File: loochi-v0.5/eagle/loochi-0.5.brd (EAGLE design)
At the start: 68.8 x 63.8 mm, 55 parts, among them IC1 ATTINY61M, J1 SPI_PRG, J2 POWER_JACKSMD, P1 53047-0610, Q1 PMN25ENSOT457, Q2 PMN25ENSOT457, Q3 PMN25ENSOT457, U1 LZ4-00MC00BIGPADS, U2 APDS-9007, X1 SMA-SMD

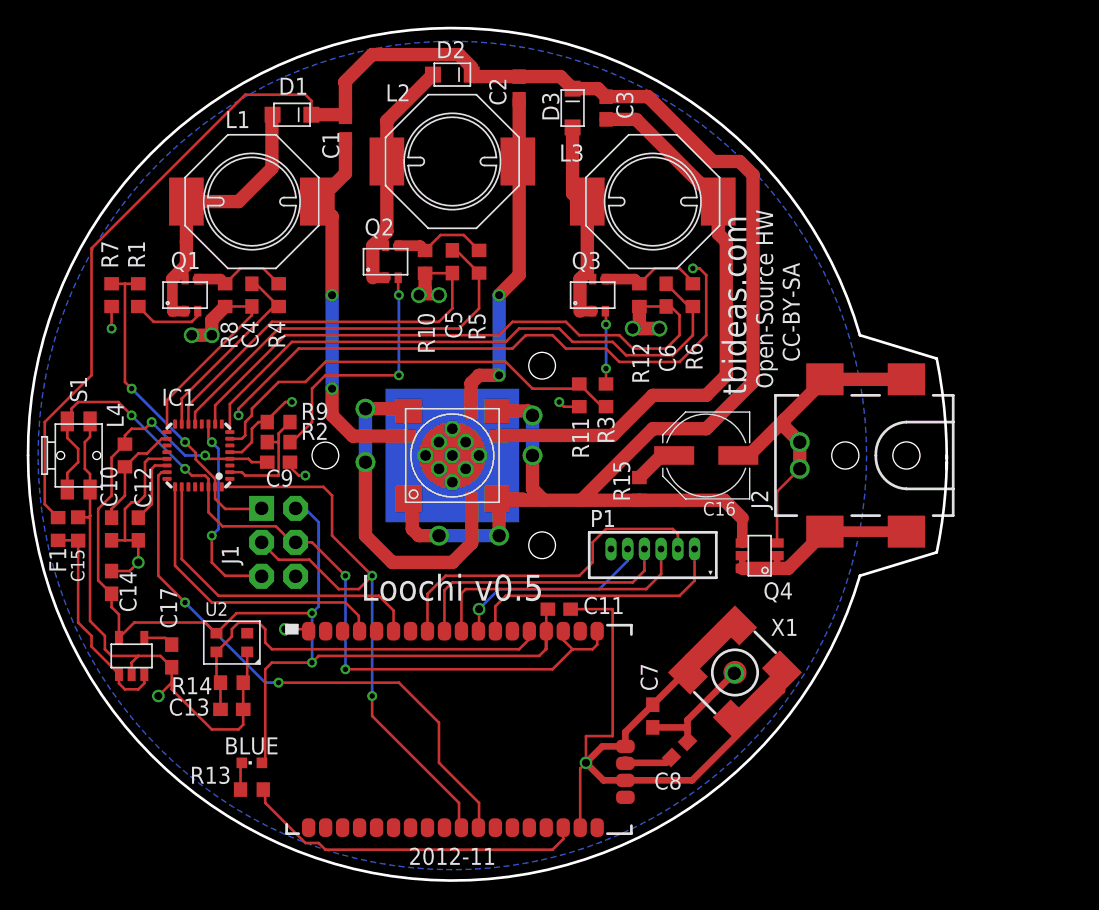
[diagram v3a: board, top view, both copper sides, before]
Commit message: Commiting board 0.5 as ordered from Oshpark.com
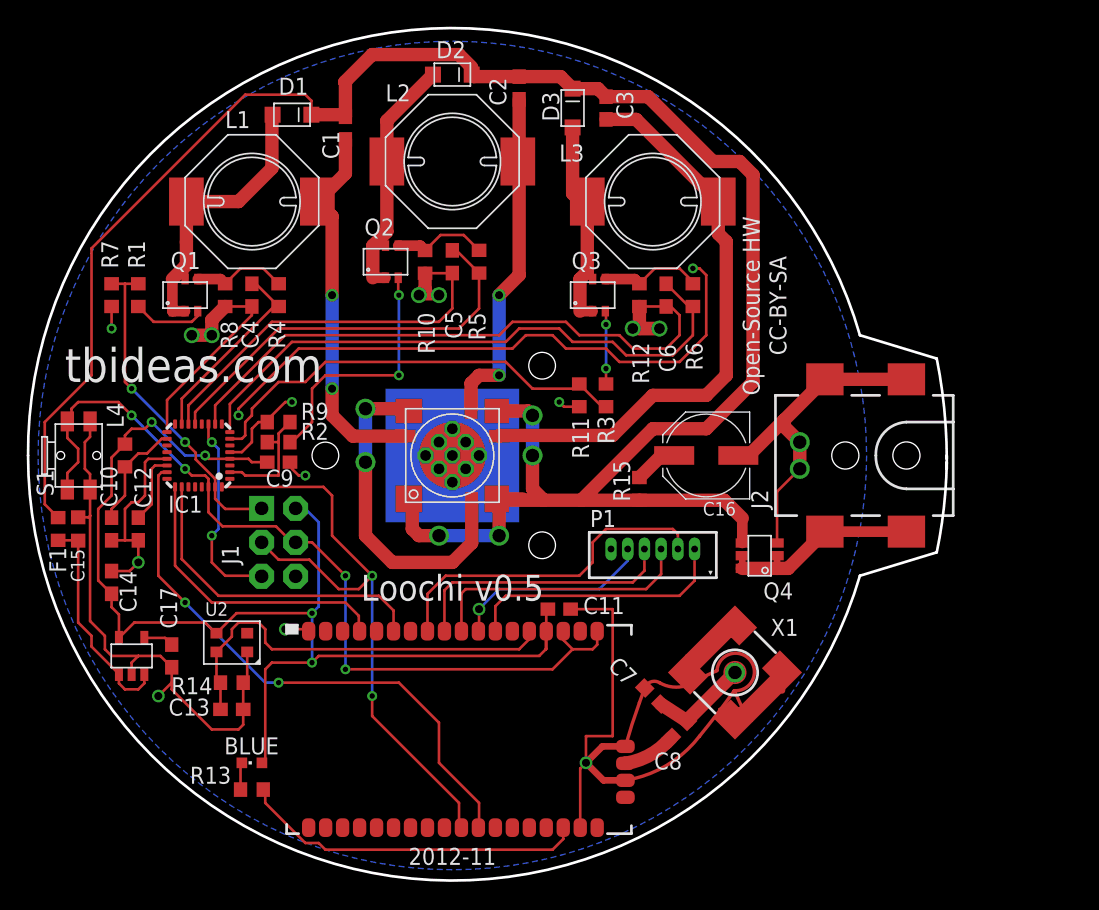
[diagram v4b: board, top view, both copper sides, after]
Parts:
- moved C7 1.50 mm to (47.0, 14.0), turned to 135 degrees
- moved C8 1.50 mm to (49.0, 11.5)
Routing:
- net GND: track 312.9 -> 317.9 mm
- net N$15: track 9.29 -> 7.51 mm, vias 0 -> 1
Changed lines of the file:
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@@
 <hole x="38.718" y="25.282" drill="2"/>
 <text x="32" y="22.1" size="1.9304" layer="21" font="vector" align="center">Loochi v0.5</text>
-<text x="54" y="36.5" size="1.778" layer="21" rot="R90">tbideas.com</text>
-<text x="56" y="37" size="1.27" layer="21" rot="R90">Open-Source HW</text>
-<text x="58" y="39" size="1.27" layer="21" rot="R90">CC-BY-SA</text>
+<text x="3" y="37.5" size="2.54" layer="21" font="vector">tbideas.com</text>
+<text x="55" y="36.5" size="1.27" layer="21" rot="R90">Open-Source HW</text>
+<text x="57" y="39.5" size="1.27" layer="21" rot="R90">CC-BY-SA</text>
 <text x="32" y="2" size="1.27" layer="21" font="vector" align="center">2012-11</text>
 <wire x1="0.25" y1="32" x2="62.5" y2="23" width="0.2" layer="20" curve="163.686148"/>
@@
 <attribute name="MF" value="" x="-37.8" y="38.35" size="1.778" layer="27" rot="R180" display="off"/>
 <attribute name="OC_FARNELL" value="unknown" x="-37.8" y="38.35" size="1.778" layer="27" rot="R180" display="off"/>
-<attribute name="NAME" x="10.24" y="35.7206" size="1.27" layer="25" ratio="10"/>
+<attribute name="NAME" x="10.74" y="27.7206" size="1.27" layer="25" ratio="10"/>
 </element>
 <element name="Q1" library="mosfet" package="SOT457" value="PMN25ENSOT457" x="12" y="44" smashed="yes" rot="R90">
@@
 <element name="S1" library="AIRcam" package="TACTSWITCHHORIZONTAL" value="" x="2.69" y="32" smashed="yes" rot="R270">
 <attribute name="PARTNO" value="*" x="11.19" y="39" size="1.778" layer="27" rot="R270" display="off"/>
-<attribute name="NAME" x="3.39" y="37.95" size="1.27" layer="25" rot="R270"/>
+<attribute name="NAME" x="0.89" y="30.95" size="1.27" layer="25" rot="R270"/>
 <attribute name="VALUE" x="0.19" y="34.25" size="0.8128" layer="27" ratio="10" rot="R270"/>
 </element>
@@
 <attribute name="VALUE" x="18.27" y="10.905" size="1.27" layer="27" rot="R180"/>
 </element>
-<element name="C8" library="rcl" package="C0603" value="100n" x="49" y="10" smashed="yes" rot="R45">
-<attribute name="PARTNO" value="*" x="49" y="10" size="1.778" layer="27" rot="R45" display="off"/>
-<attribute name="NAME" x="47.101971875" y="7" size="1.27" layer="25"/>
-</element>
-<element name="C7" library="rcl" package="C0603" value="100n" x="47" y="12.5" smashed="yes" rot="R90">
-<attribute name="PARTNO" value="*" x="47" y="12.5" size="1.778" layer="27" rot="R90" display="off"/>
-<attribute name="NAME" x="47.365" y="14.365" size="1.27" layer="25" rot="R90"/>
+<element name="C8" library="rcl" package="C0603" value="100n" x="49" y="11.5" smashed="yes" rot="R45">
+<attribute name="PARTNO" value="*" x="49" y="11.5" size="1.778" layer="27" rot="R45" display="off"/>
+<attribute name="NAME" x="47.101971875" y="8.5" size="1.27" layer="25"/>
+</element>
+<element name="C7" library="rcl" package="C0603" value="100n" x="47" y="14" smashed="yes" rot="R135">
+<attribute name="PARTNO" value="*" x="47" y="14" size="1.778" layer="27" rot="R135" display="off"/>
+<attribute name="NAME" x="45.9393375" y="15.57684375" size="1.27" layer="25" rot="R135"/>
 </element>
 <element name="R15" library="rcl" package="R0603" value="2" x="46" y="29.5" smashed="yes" rot="R270">
@@
 <wire x1="44" y1="11" x2="42" y2="11" width="0.2" layer="1"/>
 <wire x1="42" y1="11" x2="42" y2="9" width="0.2" layer="1"/>
-<wire x1="44.95" y1="10.23" x2="44.95" y2="11.3" width="0.5" layer="1"/>
-<wire x1="44.95" y1="11.3" x2="47" y2="13.35" width="0.5" layer="1"/>
 <wire x1="4.89" y1="29.45" x2="4.89" y2="27.5" width="0.2" layer="1"/>
 <wire x1="4.89" y1="27.5" x2="4.89" y2="19.61" width="0.2" layer="1"/>
@@
 <wire x1="4.5" y1="31" x2="4.89" y2="30.61" width="0.2" layer="1"/>
 <wire x1="4.89" y1="30.61" x2="4.89" y2="29.45" width="0.2" layer="1"/>
-<wire x1="49.93935625" y1="7.69" x2="44.95" y2="7.69" width="0.5" layer="1"/>
 <wire x1="15" y1="43.15" x2="14" y2="42.15" width="1" layer="1"/>
 <wire x1="14" y1="42.15" x2="14" y2="41" width="1" layer="1"/>
 <wire x1="49.63214375" y1="15.6003" x2="49.2503" y2="15.6003" width="0.5" layer="1"/>
-<wire x1="49.2503" y1="15.6003" x2="47" y2="13.35" width="0.5" layer="1"/>
 <wire x1="49.63214375" y1="15.6003" x2="49.63214375" y2="16.201340625" width="0.5" layer="1"/>
 <wire x1="49.63214375" y1="16.201340625" x2="51.1701" y2="17.739296875" width="0.5" layer="1"/>
@@
 <wire x1="56.667853125" y1="15.31745625" x2="55.129896875" y2="13.7795" width="0.5" layer="1"/>
 <wire x1="55.129896875" y1="13.7795" x2="54.52885625" y2="13.7795" width="0.5" layer="1"/>
-<wire x1="54.52885625" y1="13.7795" x2="52.9909" y2="12.24154375" width="0.5" layer="1"/>
+<wire x1="54.52885625" y1="13.7795" x2="53.74935625" y2="13" width="0.5" layer="1"/>
+<wire x1="53.74935625" y1="13" x2="52.9909" y2="12.24154375" width="0.5" layer="1"/>
 <wire x1="56.667853125" y1="15.918496875" x2="56.667853125" y2="14.418496875" width="0.5" layer="1"/>
-<wire x1="56.667853125" y1="14.418496875" x2="49.93935625" y2="7.69" width="0.5" layer="1"/>
 <wire x1="10.65" y1="31.75" x2="9.25" y2="31.75" width="0.2" layer="1"/>
 <wire x1="9.25" y1="31.75" x2="9" y2="31.5" width="0.2" layer="1"/>
@@
 <wire x1="56.3" y1="25.45" x2="56.3" y2="29.3" width="0.2" layer="1"/>
 <wire x1="56.3" y1="29.3" x2="58" y2="31" width="0.2" layer="1"/>
+<wire x1="44.95" y1="7.69" x2="50.5" y2="11" width="0.254" layer="1" curve="43.462624"/>
+<wire x1="50.5" y1="11" x2="53.1" y2="14.4" width="0.254" layer="1" curve="3.838626"/>
+<wire x1="46.39895625" y1="14.601040625" x2="46" y2="13.5" width="0.254" layer="1"/>
+<wire x1="46" y1="13.5" x2="44.95" y2="10.23" width="0.254" layer="1" curve="4.231689"/>
+<wire x1="46.39895625" y1="14.601040625" x2="47.5" y2="15" width="0.254" layer="1" curve="-100.329124"/>
+<wire x1="47.5" y1="15" x2="50" y2="15" width="0.254" layer="1" curve="60.493481"/>
+<wire x1="53.74935625" y1="13" x2="52" y2="13" width="0.254" layer="1"/>
+<wire x1="49.63214375" y1="15.6003" x2="49.83184375" y2="15.8" width="0.254" layer="1"/>
+<wire x1="53.74935625" y1="13" x2="53.1" y2="14.4" width="0.254" layer="1"/>
+<wire x1="50" y1="15" x2="51.8" y2="15.9" width="0.254" layer="1" curve="-7.363378"/>
+<wire x1="51.8" y1="15.9" x2="53.1" y2="14.4" width="0.254" layer="1" curve="-270"/>
+<wire x1="50" y1="15" x2="49.63214375" y2="15.6003" width="0" layer="19" extent="1-1"/>
 </signal>
 <signal name="V+">
@@
 <contactref element="U$1" pad="ANT"/>
 <wire x1="44.95" y1="8.96" x2="44.95" y2="9" width="1" layer="1"/>
-<wire x1="44.95" y1="9" x2="48" y2="9" width="0.5" layer="1"/>
 <contactref element="C8" pad="1"/>
-<wire x1="48.39895625" y1="9.39895625" x2="48" y2="9" width="0.5" layer="1"/>
+<wire x1="48.39895625" y1="10.89895625" x2="48" y2="10.5" width="1.016" layer="1"/>
+<wire x1="48" y1="10.5" x2="44.95" y2="8.96" width="1.016" layer="1" curve="-36.419926"/>
 </signal>
 <signal name="N$3">
@@
 <contactref element="C8" pad="2"/>
 <contactref element="C7" pad="1"/>
-<wire x1="49.601040625" y1="10.601040625" x2="49.601040625" y2="11.5" width="0.5" layer="1"/>
-<wire x1="49.601040625" y1="11.5" x2="49.601040625" y2="12.210440625" width="0.5" layer="1"/>
-<wire x1="49.601040625" y1="12.210440625" x2="53.15" y2="15.7594" width="0.5" layer="1"/>
-<wire x1="47" y1="11.65" x2="49.451040625" y2="11.65" width="0.5" layer="1"/>
-<wire x1="49.451040625" y1="11.65" x2="49.601040625" y2="11.5" width="0.5" layer="1"/>
+<wire x1="49.601040625" y1="12.210440625" x2="53.15" y2="15.7594" width="1.016" layer="1"/>
+<wire x1="47.601040625" y1="13.39895625" x2="49.601040625" y2="12.101040625" width="1.016" layer="1"/>
+<wire x1="49.601040625" y1="12.210440625" x2="49.601040625" y2="12.101040625" width="0.2" layer="1" curve="90"/>
+<via x="53.15" y="15.7594" extent="1-16" drill="1" shape="octagon"/>
+<wire x1="53.15" y1="15.7594" x2="53.15" y2="15.7594" width="0" layer="19" extent="1-1"/>
 </signal>
 <signal name="N$21">
@@
 <wire x1="5" y1="17.7" x2="7.05" y2="15.65" width="0.2" layer="1"/>
 </signal>
-<signal name="N$6">
-<via x="53.1" y="15.7" extent="1-16" drill="1" shape="octagon"/>
-</signal>
 <signal name="N$16">
